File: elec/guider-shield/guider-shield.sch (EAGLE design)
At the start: 11 parts, among them U2 PCA9536-SO8, U3 TLP291, X1 OPENMV3, X2 MTJ-663X1

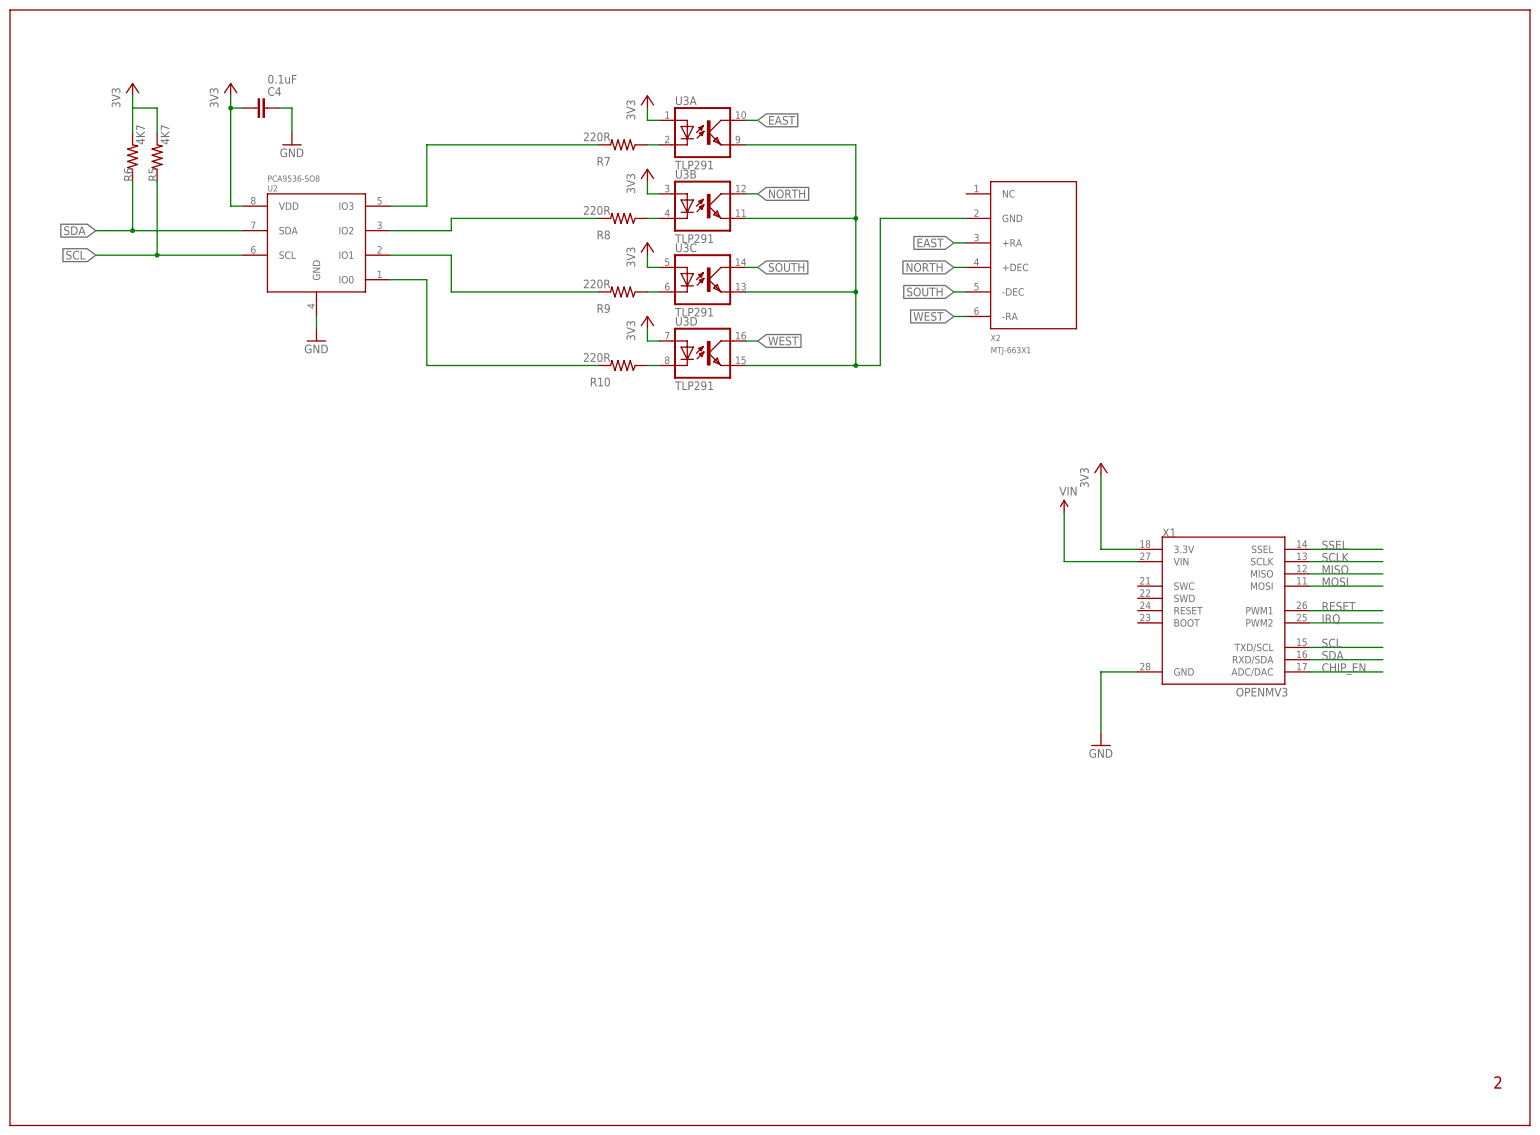
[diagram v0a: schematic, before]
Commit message: guider-shield added intervalometer output
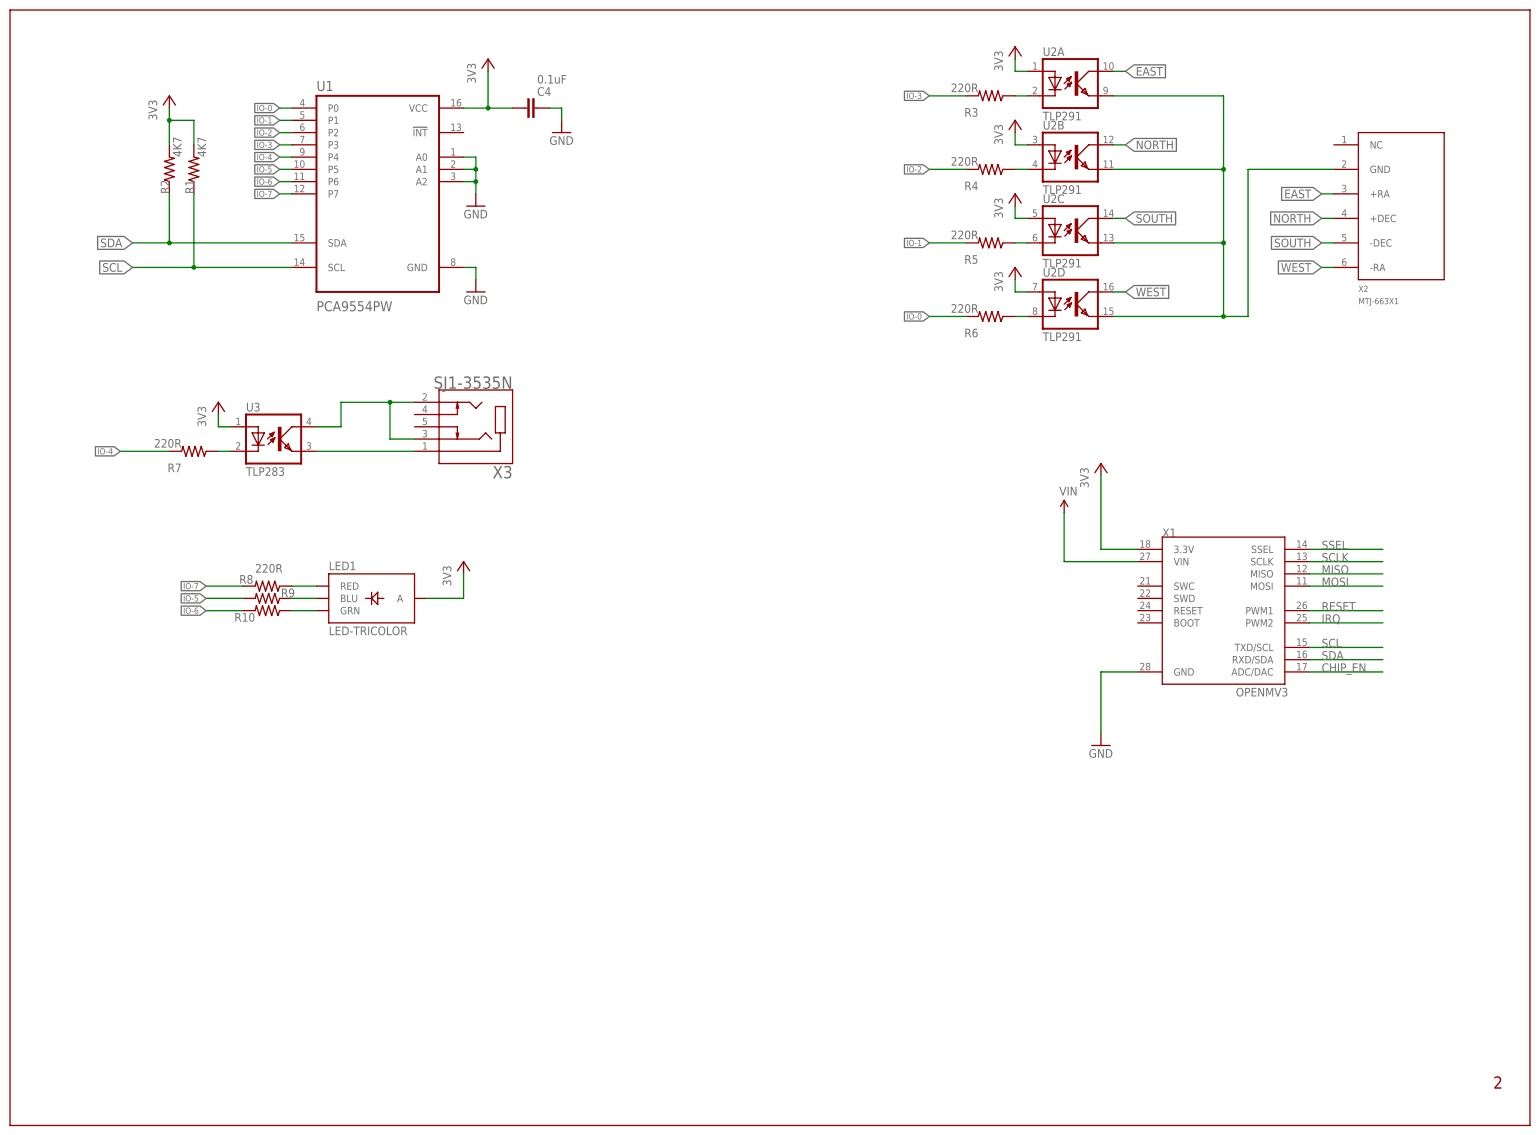
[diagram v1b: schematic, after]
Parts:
- added LED1: LED-TRICOLOR, guider-shield:LED-TRICOLOR
- added R1, R2: 4K7, sfe:RESISTOR0603-RES
- added R3, R4: 220R, sfe:RESISTOR0603-RES
- added U1: PCA9554PW, guider-shield:PCA9554PW
- added X3: SJ1-3535N, guider-shield:SJ1-3535N
- R5, R6: value 4K7 -> 220R
- U2: value PCA9536-SO8 -> TLP291; device guider-shield:PCA9536-SO8 -> guider-shield:TLP283-4-SO016
- U3: value TLP291 -> TLP283; device guider-shield:TLP283-4-SO016 -> guider-shield:TLP283
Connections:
- removed net N$22: R9.2, U2.IO1
- removed net N$23: R10.2, U2.IO0
- new net IO-0: R6.2, U1.P0
- new net IO-1: R5.2, U1.P1
- new net IO-2: R4.2, U1.P2
- new net IO-3: R3.2, U1.P3
- new net IO-4: R7.2, U1.P4
- new net IO-5: R9.2, U1.P5
- new net IO-6: R10.2, U1.P6
- new net IO-7: R8.2, U1.P7
- new net N$13: R7.1, U3.C
- new net N$14: U3.EMIT, X3.1
- new net N$15: U3.COL, X3.2, X3.3
- new net N$4: LED1.GRN, R10.1
- net 3V3: now also LED1.A, R1.2, R2.2, U1.VCC, U2A.A, U2B.A, U2C.A, U2D.A, U3.A; no longer R5.2, R6.2, U2.VDD, U3A.A, U3B.A, U3C.A, U3D.A
- net EAST: now also U2A.COL; no longer U3A.COL
- net GND: now also U1.A0, U1.A1, U1.A2, U1.GND; no longer U2.GND
- net N$1: now also LED1.RED, R8.1; no longer R7.2, U2.IO3
- net N$16: now also R4.1, U2B.C; no longer R8.1, U3B.C
- net N$2: now also LED1.BLU, R9.1; no longer R8.2, U2.IO2
- net N$20: now also R5.1, U2C.C; no longer R9.1, U3C.C
- net N$21: now also R6.1, U2D.C; no longer R10.1, U3D.C
- net N$24: now also U2A.EMIT, U2B.EMIT, U2C.EMIT, U2D.EMIT; no longer U3A.EMIT, U3B.EMIT, U3C.EMIT, U3D.EMIT
- net N$8: now also R3.1, U2A.C; no longer R7.1, U3A.C
- net NORTH: now also U2B.COL; no longer U3B.COL
- net SCL: now also R1.1, U1.SCL; no longer R5.1, U2.SCL
- net SDA: now also R2.1, U1.SDA; no longer R6.1, U2.SDA
- net SOUTH: now also U2C.COL; no longer U3C.COL
- net WEST: now also U2D.COL; no longer U3D.COL
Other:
- moved on the sheet: C4, R10, R5, R6, R7, R8, R9, X2
